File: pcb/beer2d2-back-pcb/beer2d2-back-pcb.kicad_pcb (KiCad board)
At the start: 2 copper layers, 233 parts, among them IC1 74HC238, IC2 TLC5971, IC3 FT230X, IC4 LM1117, IC5 ATMEGA328P, J1 USB, J2 PSI1, J3 PSI2, J4 RGB1, J5 RGB2, J6 6-12V, P1 AVR_ISP, Q1 DDTD113ZC, Q10 DDTB113ZC, Q11 DDTB113ZC, Q12 DDTB113ZC, Q13 DDTB113ZC, Q14 DDTB113ZC, Q15 DDTB113ZC, Q16 DDTB113ZC, Q17 DDTB113ZC, Q18 DDTB113ZC, Q19 DDTB113ZC, Q2 DDTD113ZC, Q3 DDTD113ZC, Q4 DDTD113ZC, Q5 DDTD113ZC, Q6 DDTD113ZC, Q7 DDTD113ZC, Q8 DDTD113ZC, Q9 DDTB113ZC, Y1 16MHz

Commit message: tentative placement layout
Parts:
- removed R10, R12, R14, R16, R18, R20, R22, R24, R26, R28, R29, R30, R31, R32, R33, R34, R35, R36, R37, R38, R39, R40, R41, R42, R43, R44, R45, R46, R47, R48, R49, R50, R51, R52, R53, R54, R55, R56, R57, R58, R59, R60, R61, R62, R63, R64, R65, R66, R67, R68, R69, R70, R71, R72, R73, R74, R75, R76, R77, R78, R79, R8, R80, R81, R82, R83, R84, R85, R86, R87, R88, R89, R90, R91, R92, R93, R94: 110Ω, general sm:0603(1608m)
- moved J1 211.6 mm to (257.2, 112.4), turned to 180 degrees
- moved LED17 205.2 mm to (250.2, 90.8)
- moved LED18 203.2 mm to (250.2, 96.5)
- moved LED26 203.2 mm to (244.5, 96.5)
- moved LED24 199.8 mm to (244.5, 85.1)
- moved LED15 199.2 mm to (250.2, 79.4)
- moved LED25 198.4 mm to (244.5, 90.8)
- moved LED16 195.4 mm to (250.2, 85.1)
- moved LED23 190.4 mm to (244.5, 79.4)
- moved LED10 187.0 mm to (255.9, 96.5)
- moved IC3 185.1 mm to (243.8, 111.1), turned to 270 degrees
- moved R3 181.5 mm to (250.8, 111.8), turned to 180 degrees
- moved LED40 181.4 mm to (233.0, 85.1)
- moved LED32 180.4 mm to (238.8, 85.1)
- moved LED34 179.0 mm to (238.8, 96.5)
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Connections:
- IC2 pad 11: Net-(IC2-Pad11) -> (no net)
- IC2 pad 12: Net-(IC2-Pad12) -> (no net)
- IC3 pad 15: Net-(IC3-Pad15) -> (no net)
- IC3 pad 6: Net-(IC3-Pad6) -> (no net)
- IC5 pad 19: Net-(IC5-Pad19) -> (no net)
- IC5 pad 22: Net-(IC5-Pad22) -> (no net)
- IC5 pad 26: Net-(IC5-Pad26) -> (no net)
- J1 pad 4: Net-(J1-Pad4) -> (no net)
- LED10 pad 1: Net-(LED10-Pad1) -> /LED Matrix/ROW7
- LED10 pad 2: /LED Matrix/COL0 -> N-0000097
- LED11 pad 1: Net-(LED11-Pad1) -> /LED Matrix/ROW0
- LED11 pad 2: /LED Matrix/COL1 -> N-0000096
- LED12 pad 1: Net-(LED12-Pad1) -> /LED Matrix/ROW1
- LED12 pad 2: /LED Matrix/COL1 -> N-0000096
- LED13 pad 1: Net-(LED13-Pad1) -> /LED Matrix/ROW2
- LED13 pad 2: /LED Matrix/COL1 -> N-0000096
- LED14 pad 1: Net-(LED14-Pad1) -> /LED Matrix/ROW3
- LED14 pad 2: /LED Matrix/COL1 -> N-0000096
- LED15 pad 1: Net-(LED15-Pad1) -> /LED Matrix/ROW4
- LED15 pad 2: /LED Matrix/COL1 -> N-0000096
- LED16 pad 1: Net-(LED16-Pad1) -> /LED Matrix/ROW5
- LED16 pad 2: /LED Matrix/COL1 -> N-0000096
- LED17 pad 1: Net-(LED17-Pad1) -> /LED Matrix/ROW6
- LED17 pad 2: /LED Matrix/COL1 -> N-0000096
- LED18 pad 1: Net-(LED18-Pad1) -> /LED Matrix/ROW7
- LED18 pad 2: /LED Matrix/COL1 -> N-0000096
- LED19 pad 1: Net-(LED19-Pad1) -> /LED Matrix/ROW0
- LED19 pad 2: /LED Matrix/COL2 -> N-0000098
- LED20 pad 1: Net-(LED20-Pad1) -> /LED Matrix/ROW1
- LED20 pad 2: /LED Matrix/COL2 -> N-0000098
- LED21 pad 1: Net-(LED21-Pad1) -> /LED Matrix/ROW2
- LED21 pad 2: /LED Matrix/COL2 -> N-0000098
- LED22 pad 1: Net-(LED22-Pad1) -> /LED Matrix/ROW3
- LED22 pad 2: /LED Matrix/COL2 -> N-0000098
- LED23 pad 1: Net-(LED23-Pad1) -> /LED Matrix/ROW4
- LED23 pad 2: /LED Matrix/COL2 -> N-0000098
- LED24 pad 1: Net-(LED24-Pad1) -> /LED Matrix/ROW5
- LED24 pad 2: /LED Matrix/COL2 -> N-0000098
- LED25 pad 1: Net-(LED25-Pad1) -> /LED Matrix/ROW6
- LED25 pad 2: /LED Matrix/COL2 -> N-0000098
- LED26 pad 1: Net-(LED26-Pad1) -> /LED Matrix/ROW7
- LED26 pad 2: /LED Matrix/COL2 -> N-0000098
- LED27 pad 1: Net-(LED27-Pad1) -> /LED Matrix/ROW0
- LED27 pad 2: /LED Matrix/COL3 -> N-0000094
- LED28 pad 1: Net-(LED28-Pad1) -> /LED Matrix/ROW1
- LED28 pad 2: /LED Matrix/COL3 -> N-0000094
- LED29 pad 1: Net-(LED29-Pad1) -> /LED Matrix/ROW2
- LED29 pad 2: /LED Matrix/COL3 -> N-0000094
- LED3 pad 1: Net-(LED3-Pad1) -> /LED Matrix/ROW0
- LED3 pad 2: /LED Matrix/COL0 -> N-0000097
- LED30 pad 1: Net-(LED30-Pad1) -> /LED Matrix/ROW3
- LED30 pad 2: /LED Matrix/COL3 -> N-0000094
- LED31 pad 1: Net-(LED31-Pad1) -> /LED Matrix/ROW4
- LED31 pad 2: /LED Matrix/COL3 -> N-0000094
- LED32 pad 1: Net-(LED32-Pad1) -> /LED Matrix/ROW5
- LED32 pad 2: /LED Matrix/COL3 -> N-0000094
- LED33 pad 1: Net-(LED33-Pad1) -> /LED Matrix/ROW6
- LED33 pad 2: /LED Matrix/COL3 -> N-0000094
- LED34 pad 1: Net-(LED34-Pad1) -> /LED Matrix/ROW7
- LED34 pad 2: /LED Matrix/COL3 -> N-0000094
- LED35 pad 1: Net-(LED35-Pad1) -> /LED Matrix/ROW0
- LED35 pad 2: /LED Matrix/COL4 -> N-0000093
- LED36 pad 1: Net-(LED36-Pad1) -> /LED Matrix/ROW1
- LED36 pad 2: /LED Matrix/COL4 -> N-0000093
- LED37 pad 1: Net-(LED37-Pad1) -> /LED Matrix/ROW2
- LED37 pad 2: /LED Matrix/COL4 -> N-0000093
- LED38 pad 1: Net-(LED38-Pad1) -> /LED Matrix/ROW3
- LED38 pad 2: /LED Matrix/COL4 -> N-0000093
- LED39 pad 1: Net-(LED39-Pad1) -> /LED Matrix/ROW4
- LED39 pad 2: /LED Matrix/COL4 -> N-0000093
- LED4 pad 1: Net-(LED4-Pad1) -> /LED Matrix/ROW1
- LED4 pad 2: /LED Matrix/COL0 -> N-0000097
- LED40 pad 1: Net-(LED40-Pad1) -> /LED Matrix/ROW5
- LED40 pad 2: /LED Matrix/COL4 -> N-0000093
- LED41 pad 1: Net-(LED41-Pad1) -> /LED Matrix/ROW6
- LED41 pad 2: /LED Matrix/COL4 -> N-0000093
- LED42 pad 1: Net-(LED42-Pad1) -> /LED Matrix/ROW7
- LED42 pad 2: /LED Matrix/COL4 -> N-0000093
- LED43 pad 1: Net-(LED43-Pad1) -> /LED Matrix/ROW0
- LED43 pad 2: /LED Matrix/COL5 -> N-0000095
- LED44 pad 1: Net-(LED44-Pad1) -> /LED Matrix/ROW1
- LED44 pad 2: /LED Matrix/COL5 -> N-0000095
- LED45 pad 1: Net-(LED45-Pad1) -> /LED Matrix/ROW2
- LED45 pad 2: /LED Matrix/COL5 -> N-0000095
- LED46 pad 1: Net-(LED46-Pad1) -> /LED Matrix/ROW3
- LED46 pad 2: /LED Matrix/COL5 -> N-0000095
- LED47 pad 1: Net-(LED47-Pad1) -> /LED Matrix/ROW4
- LED47 pad 2: /LED Matrix/COL5 -> N-0000095
- LED48 pad 1: Net-(LED48-Pad1) -> /LED Matrix/ROW5
- LED48 pad 2: /LED Matrix/COL5 -> N-0000095
- LED49 pad 1: Net-(LED49-Pad1) -> /LED Matrix/ROW6
- LED49 pad 2: /LED Matrix/COL5 -> N-0000095
- LED5 pad 1: Net-(LED5-Pad1) -> /LED Matrix/ROW2
- LED5 pad 2: /LED Matrix/COL0 -> N-0000097
- LED50 pad 1: Net-(LED50-Pad1) -> /LED Matrix/ROW7
- LED50 pad 2: /LED Matrix/COL5 -> N-0000095
- LED51 pad 1: Net-(LED51-Pad1) -> /LED Matrix/ROW0
- LED51 pad 2: /LED Matrix/COL6 -> N-0000081
- LED52 pad 1: Net-(LED52-Pad1) -> /LED Matrix/ROW1
- LED52 pad 2: /LED Matrix/COL6 -> N-0000081
- LED53 pad 1: Net-(LED53-Pad1) -> /LED Matrix/ROW2
- LED53 pad 2: /LED Matrix/COL6 -> N-0000081
- LED54 pad 1: Net-(LED54-Pad1) -> /LED Matrix/ROW3
- LED54 pad 2: /LED Matrix/COL6 -> N-0000081
- LED55 pad 1: Net-(LED55-Pad1) -> /LED Matrix/ROW4
- LED55 pad 2: /LED Matrix/COL6 -> N-0000081
- LED56 pad 1: Net-(LED56-Pad1) -> /LED Matrix/ROW5
- LED56 pad 2: /LED Matrix/COL6 -> N-0000081
- LED57 pad 1: Net-(LED57-Pad1) -> /LED Matrix/ROW6
- LED57 pad 2: /LED Matrix/COL6 -> N-0000081
- LED58 pad 1: Net-(LED58-Pad1) -> /LED Matrix/ROW7
- LED58 pad 2: /LED Matrix/COL6 -> N-0000081
- LED59 pad 1: Net-(LED59-Pad1) -> /LED Matrix/ROW0
- LED59 pad 2: /LED Matrix/COL7 -> N-0000082
- LED6 pad 1: Net-(LED6-Pad1) -> /LED Matrix/ROW3
- LED6 pad 2: /LED Matrix/COL0 -> N-0000097
- LED60 pad 1: Net-(LED60-Pad1) -> /LED Matrix/ROW1
- LED60 pad 2: /LED Matrix/COL7 -> N-0000082
- LED61 pad 1: Net-(LED61-Pad1) -> /LED Matrix/ROW2
- LED61 pad 2: /LED Matrix/COL7 -> N-0000082
- LED62 pad 1: Net-(LED62-Pad1) -> /LED Matrix/ROW3
- LED62 pad 2: /LED Matrix/COL7 -> N-0000082
- LED63 pad 1: Net-(LED63-Pad1) -> /LED Matrix/ROW4
- LED63 pad 2: /LED Matrix/COL7 -> N-0000082
- LED64 pad 1: Net-(LED64-Pad1) -> /LED Matrix/ROW5
- LED64 pad 2: /LED Matrix/COL7 -> N-0000082
- LED65 pad 1: Net-(LED65-Pad1) -> /LED Matrix/ROW6
- LED65 pad 2: /LED Matrix/COL7 -> N-0000082
- LED66 pad 1: Net-(LED66-Pad1) -> /LED Matrix/ROW7
- LED66 pad 2: /LED Matrix/COL7 -> N-0000082
- LED67 pad 1: Net-(LED67-Pad1) -> /LED Matrix/ROW0
- LED67 pad 2: /LED Matrix/COL8 -> N-0000080
- LED68 pad 1: Net-(LED68-Pad1) -> /LED Matrix/ROW1
- LED68 pad 2: /LED Matrix/COL8 -> N-0000080
- LED69 pad 1: Net-(LED69-Pad1) -> /LED Matrix/ROW2
- LED69 pad 2: /LED Matrix/COL8 -> N-0000080
- LED7 pad 1: Net-(LED7-Pad1) -> /LED Matrix/ROW4
- LED7 pad 2: /LED Matrix/COL0 -> N-0000097
- LED70 pad 1: Net-(LED70-Pad1) -> /LED Matrix/ROW3
- LED70 pad 2: /LED Matrix/COL8 -> N-0000080
- LED71 pad 1: Net-(LED71-Pad1) -> /LED Matrix/ROW4
- LED71 pad 2: /LED Matrix/COL8 -> N-0000080
- LED72 pad 1: Net-(LED72-Pad1) -> /LED Matrix/ROW5
- LED72 pad 2: /LED Matrix/COL8 -> N-0000080
- LED73 pad 1: Net-(LED73-Pad1) -> /LED Matrix/ROW6
- LED73 pad 2: /LED Matrix/COL8 -> N-0000080
- LED74 pad 1: Net-(LED74-Pad1) -> /LED Matrix/ROW7
- LED74 pad 2: /LED Matrix/COL8 -> N-0000080
- LED75 pad 1: Net-(LED75-Pad1) -> /LED Matrix/ROW0
- LED75 pad 2: /LED Matrix/COL9 -> N-0000085
- LED76 pad 1: Net-(LED76-Pad1) -> /LED Matrix/ROW1
- LED76 pad 2: /LED Matrix/COL9 -> N-0000085
- LED77 pad 1: Net-(LED77-Pad1) -> /LED Matrix/ROW2
- LED77 pad 2: /LED Matrix/COL9 -> N-0000085
- LED78 pad 1: Net-(LED78-Pad1) -> /LED Matrix/ROW3
- LED78 pad 2: /LED Matrix/COL9 -> N-0000085
- LED79 pad 1: Net-(LED79-Pad1) -> /LED Matrix/ROW4
- LED79 pad 2: /LED Matrix/COL9 -> N-0000085
- LED8 pad 1: Net-(LED8-Pad1) -> /LED Matrix/ROW5
- LED8 pad 2: /LED Matrix/COL0 -> N-0000097
- LED80 pad 1: Net-(LED80-Pad1) -> /LED Matrix/ROW5
- LED80 pad 2: /LED Matrix/COL9 -> N-0000085
- LED81 pad 1: Net-(LED81-Pad1) -> /LED Matrix/ROW6
- LED81 pad 2: /LED Matrix/COL9 -> N-0000085
- LED82 pad 1: Net-(LED82-Pad1) -> /LED Matrix/ROW7
- LED82 pad 2: /LED Matrix/COL9 -> N-0000085
- LED83 pad 1: Net-(LED83-Pad1) -> /LED Matrix/ROW0
- LED83 pad 2: /LED Matrix/COL10 -> N-0000074
- LED84 pad 1: Net-(LED84-Pad1) -> /LED Matrix/ROW1
- LED84 pad 2: /LED Matrix/COL10 -> N-0000074
- LED85 pad 1: Net-(LED85-Pad1) -> /LED Matrix/ROW2
- LED85 pad 2: /LED Matrix/COL10 -> N-0000074
- LED86 pad 1: Net-(LED86-Pad1) -> /LED Matrix/ROW3
- LED86 pad 2: /LED Matrix/COL10 -> N-0000074
- LED87 pad 1: Net-(LED87-Pad1) -> /LED Matrix/ROW4
- LED87 pad 2: /LED Matrix/COL10 -> N-0000074
- LED88 pad 1: Net-(LED88-Pad1) -> /LED Matrix/ROW5
- LED88 pad 2: /LED Matrix/COL10 -> N-0000074
- LED89 pad 1: Net-(LED89-Pad1) -> /LED Matrix/ROW6
- LED89 pad 2: /LED Matrix/COL10 -> N-0000074
- LED9 pad 1: Net-(LED9-Pad1) -> /LED Matrix/ROW6
- LED9 pad 2: /LED Matrix/COL0 -> N-0000097
- LED90 pad 1: Net-(LED90-Pad1) -> /LED Matrix/ROW7
- LED90 pad 2: /LED Matrix/COL10 -> N-0000074
- R11 pad 1: /LED Matrix/ROW4 -> /LED Matrix/COL2
- R11 pad 2: Net-(LED7-Pad1) -> N-0000098
- R13 pad 1: /LED Matrix/ROW6 -> /LED Matrix/COL3
- R13 pad 2: Net-(LED9-Pad1) -> N-0000094
- R15 pad 1: /LED Matrix/ROW0 -> /LED Matrix/COL4
- R15 pad 2: Net-(LED11-Pad1) -> N-0000093
- R17 pad 1: /LED Matrix/ROW2 -> /LED Matrix/COL5
- R17 pad 2: Net-(LED13-Pad1) -> N-0000095
- R19 pad 1: /LED Matrix/ROW4 -> /LED Matrix/COL6
- R19 pad 2: Net-(LED15-Pad1) -> N-0000081
- R21 pad 1: /LED Matrix/ROW6 -> /LED Matrix/COL7
- R21 pad 2: Net-(LED17-Pad1) -> N-0000082
- R23 pad 1: /LED Matrix/ROW0 -> /LED Matrix/COL8
- R23 pad 2: Net-(LED19-Pad1) -> N-0000080
- R25 pad 1: /LED Matrix/ROW2 -> /LED Matrix/COL9
- R25 pad 2: Net-(LED21-Pad1) -> N-0000085
- R27 pad 1: /LED Matrix/ROW4 -> /LED Matrix/COL10
- R27 pad 2: Net-(LED23-Pad1) -> N-0000074
- R7 pad 1: /LED Matrix/ROW0 -> /LED Matrix/COL0
- R7 pad 2: Net-(LED3-Pad1) -> N-0000097
- R9 pad 1: /LED Matrix/ROW2 -> /LED Matrix/COL1
- R9 pad 2: Net-(LED5-Pad1) -> N-0000096
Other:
- board outline added: 126.4 x 41.3 mm
- board text added: "[+](r-)(b-)(g-)"

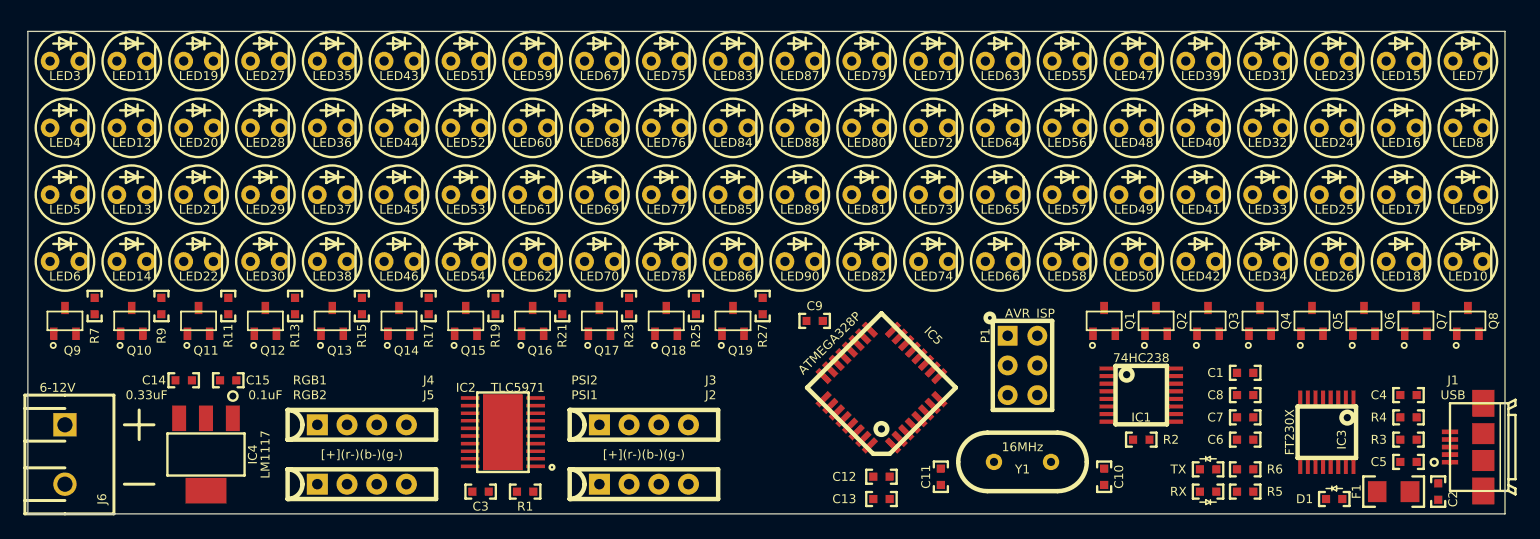
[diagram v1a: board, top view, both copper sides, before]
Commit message: continue routing for back pcb
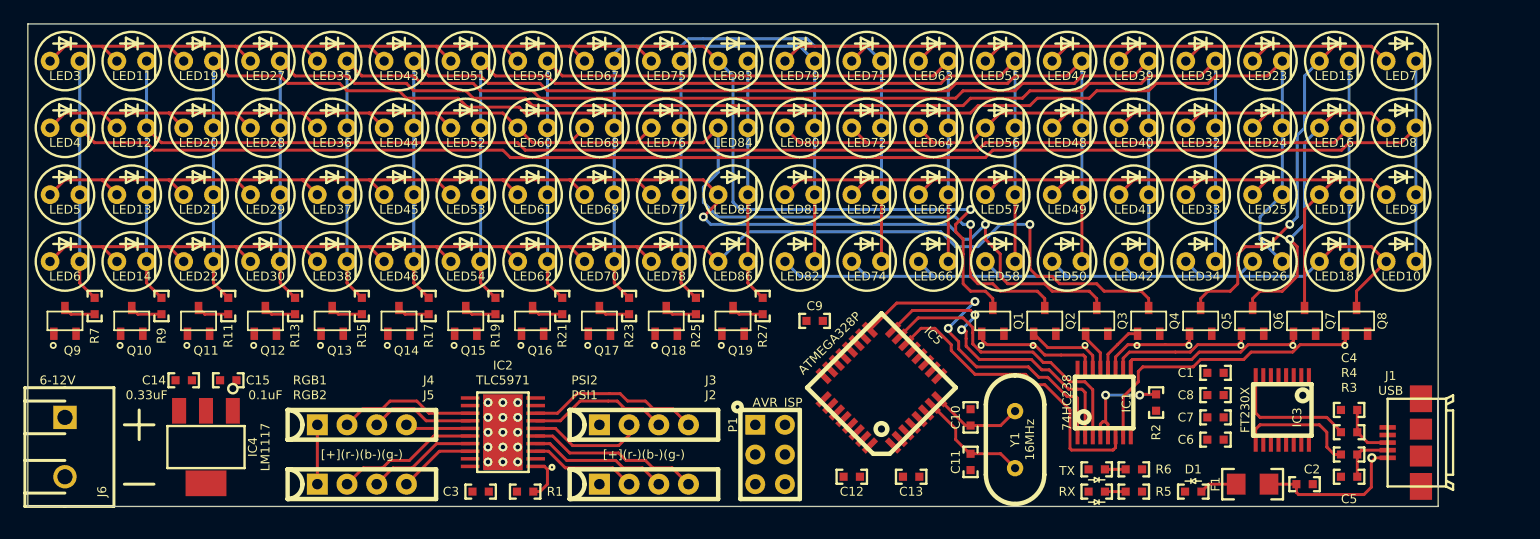
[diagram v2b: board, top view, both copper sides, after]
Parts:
- removed LED87, LED88, LED89, LED90: LED, th leds:LED-5mm
- moved P1 22.9 mm to (196.2, 113.0)
- moved C10 12.5 mm to (213.4, 109.9), turned to 270 degrees
- moved D1 12.1 mm to (232.4, 116.2)
- moved F1 12.1 mm to (237.5, 115.6)
- moved C2 11.4 mm to (241.9, 115.6), turned to 0 degrees
- moved LED1 9.53 mm to (224.2, 116.2)
- moved LED2 9.53 mm to (224.2, 114.3), turned to 180 degrees
- moved Q1 9.53 mm to (215.3, 101.6)
- moved Q2 9.53 mm to (219.7, 101.6)
- moved Q3 9.53 mm to (224.2, 101.6)
- moved Q4 9.53 mm to (228.6, 101.6)
- moved Q5 9.53 mm to (233.0, 101.6)
- moved Q7 9.53 mm to (241.9, 101.6)
- moved Q8 9.53 mm to (246.4, 101.6)
- moved Q6 9.52 mm to (237.5, 101.6)
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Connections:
- IC2 pad 11: (no net) -> Net-(IC2-Pad11)
- IC2 pad 12: (no net) -> Net-(IC2-Pad12)
- IC3 pad 15: (no net) -> Net-(IC3-Pad15)
- IC3 pad 6: (no net) -> Net-(IC3-Pad6)
- IC5 pad 19: (no net) -> Net-(IC5-Pad19)
- IC5 pad 22: (no net) -> Net-(IC5-Pad22)
- IC5 pad 26: (no net) -> Net-(IC5-Pad26)
- J1 pad 4: (no net) -> Net-(J1-Pad4)
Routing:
- net Net-(LED10-Pad2): track 0.00 -> 154.3 mm
- net Net-(LED11-Pad2): track 0.00 -> 142.4 mm
- net Net-(LED19-Pad2): track 0.00 -> 134.6 mm
- net Net-(LED27-Pad2): track 0.00 -> 121.1 mm
- net /LED Matrix/ROW3: track 0.00 -> 119.2 mm, vias 0 -> 1
- net /LED Matrix/ROW0: track 0.00 -> 118.6 mm, vias 0 -> 1
- net /LED Matrix/ROW2: track 0.00 -> 117.1 mm, vias 0 -> 2
- net /LED Matrix/ROW1: track 0.00 -> 116.5 mm, vias 0 -> 1
- net Net-(LED35-Pad2): track 0.00 -> 109.1 mm
- net Net-(LED43-Pad2): track 0.00 -> 97.2 mm
- net /LED Matrix/ROW4: track 0.00 -> 94.4 mm, vias 0 -> 1
- net /LED Matrix/ROW5: track 0.00 -> 85.7 mm, vias 0 -> 1
- net Net-(LED51-Pad2): track 0.00 -> 85.2 mm
- net /LED Matrix/ROW6: track 0.00 -> 77.1 mm
- net Net-(LED59-Pad2): track 0.00 -> 73.3 mm
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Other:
- board size 126.4 x 41.3 mm -> 120.7 x 41.3 mm

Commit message: commit for safety
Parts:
- moved C12 6.48 mm to (209.6, 113.7), turned to 90 degrees
- moved C13 3.42 mm to (211.5, 113.7), turned to 90 degrees
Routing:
- net GND: track 24.5 -> 34.3 mm
- net VCC: track 5.08 -> 12.7 mm

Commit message: commit for dinner
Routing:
- net /AVR_MISO: track 26.9 -> 57.4 mm
- net /AVR_SCK: track 30.5 -> 54.6 mm
- net /AVR_MOSI: track 24.5 -> 47.3 mm, vias 0 -> 2
- net /LED Matrix/AVR_C8: track 0.00 -> 22.6 mm, vias 0 -> 2
- net /LED Matrix/AVR_C9: track 0.00 -> 16.8 mm, vias 0 -> 2
- net /LED Matrix/AVR_C7: track 0.00 -> 15.1 mm
- net /LED Matrix/AVR_C10: track 0.00 -> 12.7 mm
- net /AVR_RST: track 0.00 -> 10.2 mm

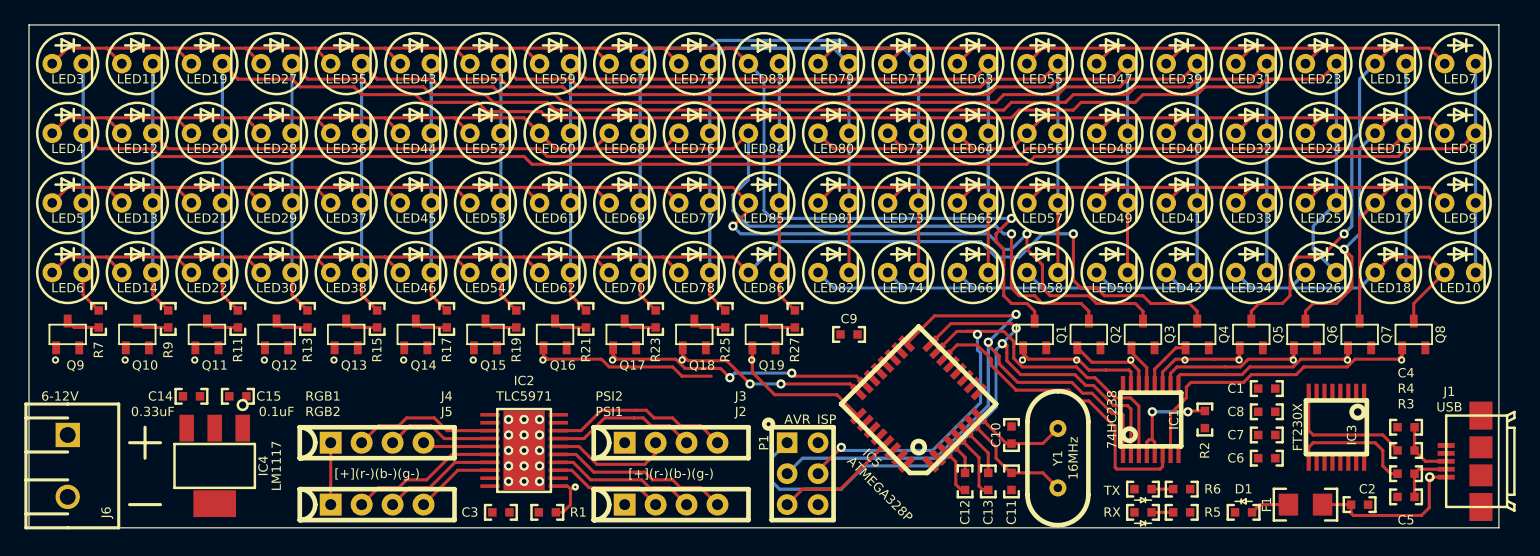
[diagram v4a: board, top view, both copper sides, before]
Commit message: layout back board copper
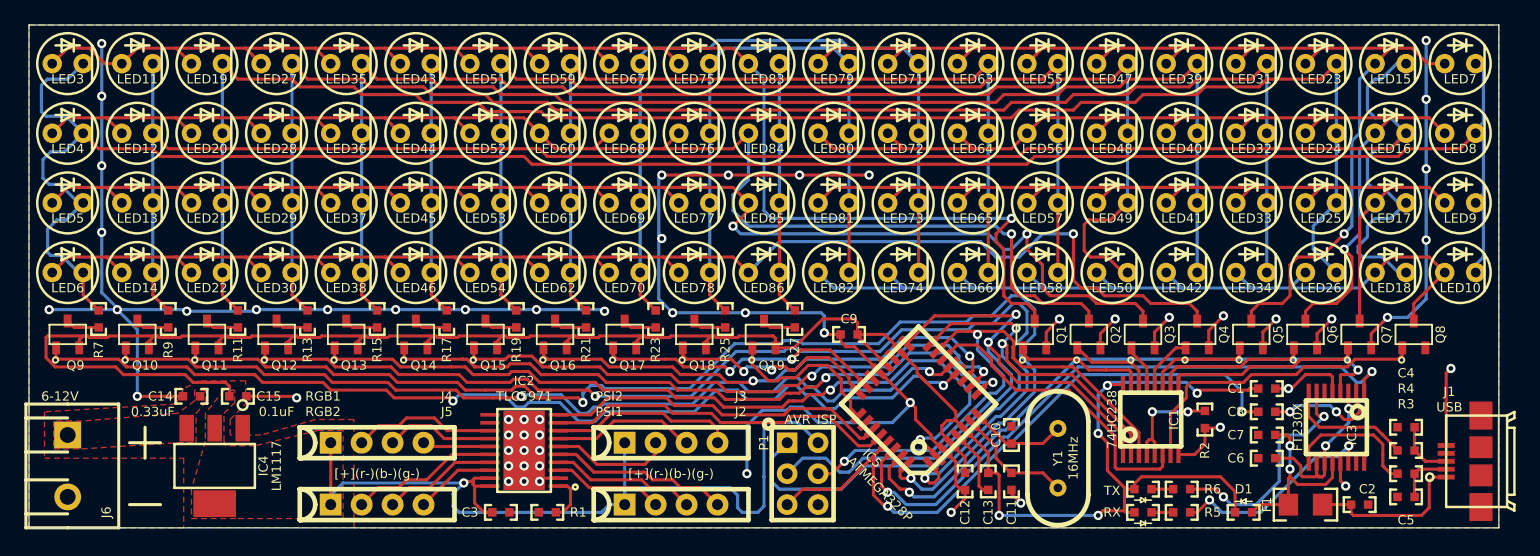
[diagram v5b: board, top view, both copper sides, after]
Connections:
- IC5 pad 27: /RGB_SDA -> /RGB_SCK
- IC5 pad 28: /RGB_SCK -> /RGB_SDA
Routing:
- net VCC: track 12.7 -> 254.1 mm, vias 0 -> 6
- net GND: track 34.3 -> 272.8 mm, vias 15 -> 57
- net /LED Matrix/AVR_C2: track 0.00 -> 100.1 mm, vias 0 -> 2
- net /LED Matrix/AVR_C3: track 0.00 -> 90.2 mm, vias 0 -> 2
- net /LED Matrix/AVR_C0: track 0.00 -> 82.2 mm, vias 0 -> 2
- net /LED Matrix/AVR_C1: track 0.00 -> 74.9 mm, vias 0 -> 2
- net /LED Matrix/AVR_C4: track 0.00 -> 65.9 mm, vias 0 -> 2
- net /LED Matrix/AVR_C5: track 0.00 -> 55.2 mm, vias 0 -> 2
- net /AVR_RX: track 0.00 -> 51.7 mm, vias 0 -> 2
- net /AVR_TX: track 0.00 -> 49.2 mm, vias 0 -> 2
- net /LED Matrix/AVR_C6: track 0.00 -> 48.2 mm, vias 0 -> 2
- net /AVR_RST: track 10.2 -> 52.5 mm, vias 0 -> 2
- net /RGB_SDA: track 0.00 -> 29.0 mm
- net /RGB_SCK: track 0.00 -> 28.4 mm
- net /LED Matrix/AVR_C7: track 15.1 -> 40.9 mm, vias 0 -> 2
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- added copper zone on B.Cu, net GND
- added copper zone on F.Cu, net GND
- added copper zone on F.Cu, net Net-(C14-Pad1)
- added copper zone on F.Cu, net VCC

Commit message: layout finished
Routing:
- net GND: track 272.8 -> 282.2 mm, vias 57 -> 58
- net Net-(IC3-Pad7): track 18.9 -> 21.3 mm
- net Net-(IC3-Pad14): track 17.5 -> 18.2 mm

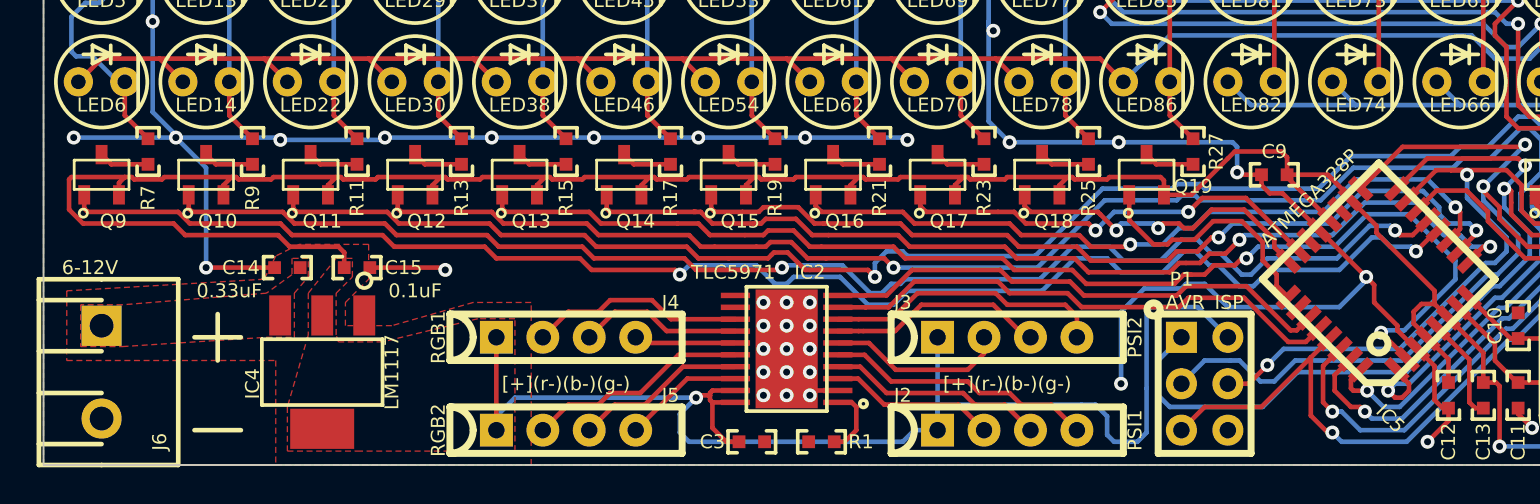
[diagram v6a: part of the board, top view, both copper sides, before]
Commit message: fix voltage regulator cap values and footprints
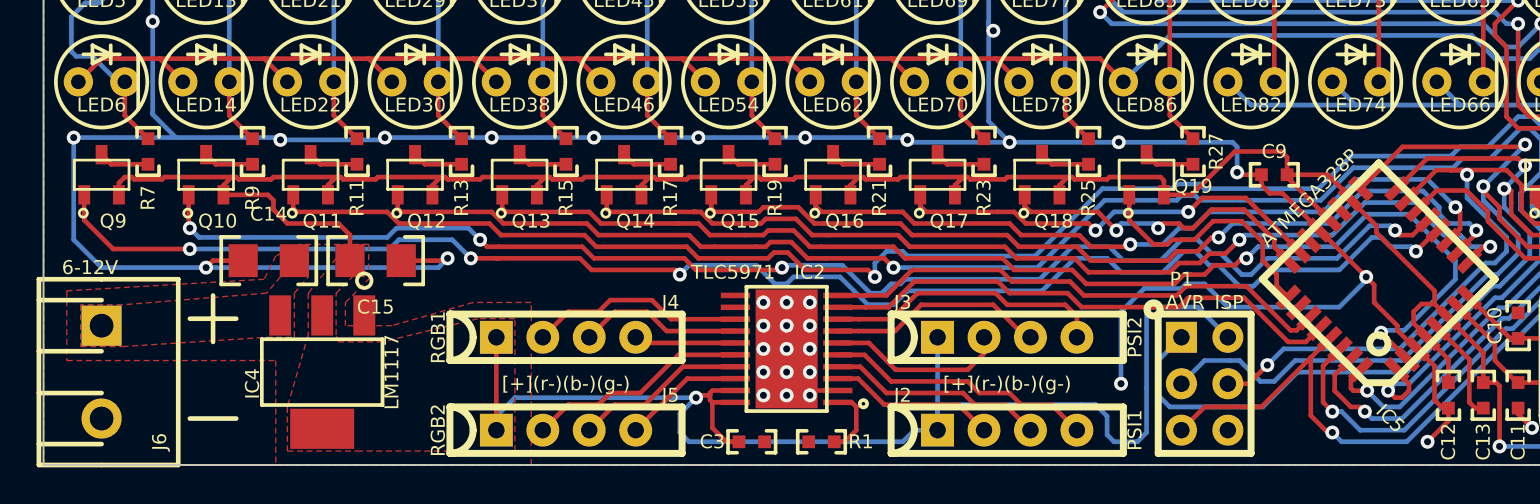
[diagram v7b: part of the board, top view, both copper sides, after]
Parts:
- C14: value 0.33uF -> 10uF; footprint general sm:0603(1608m) -> passive-smd:1206(3216m)
- C15: value 0.1uF -> 22uF; footprint general sm:0603(1608m) -> passive-smd:1206(3216m)
- moved C14 1.09 mm to (145.0, 106.3)
- moved C15 1.09 mm to (150.9, 106.3)
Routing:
- net GND: track 282.2 -> 303.8 mm, vias 58 -> 57
- net VCC: track 254.1 -> 242.0 mm
- net /LED Matrix/AVR_C0: track 82.2 -> 83.3 mm, vias 2 -> 4
- net /LED Matrix/AVR_C1: track 74.9 -> 76.0 mm, vias 2 -> 4
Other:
- board text added: "6-12V"
- board text added: "designed by wiley cousins for barton gilley because he's a cool dude"
- board text added: "rear head panel mjc 2014-04-01 open source hardware: cc by-sa 4.0 github.com/mcous/r2dbrew"
